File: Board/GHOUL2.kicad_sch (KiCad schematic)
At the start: 22 parts, among them U1 Teensy4.1, U2 DS18S20

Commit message: fixed more of JB's mistakes
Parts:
- R2: value 10K -> 15K
- R3: value 15K -> 10K
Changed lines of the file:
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@@
       (effects (font (size 1.27 1.27)) (justify left))
     )
-    (property "Value" "15K" (at 161.29 164.465 0)
+    (property "Value" "10K" (at 161.29 164.465 0)
       (effects (font (size 1.27 1.27)) (justify left))
     )
@@
       (effects (font (size 1.27 1.27)) (justify left))
     )
-    (property "Value" "10K" (at 161.29 154.305 0)
-      (effects (font (size 1.27 1.27)) (justify left))
-    )
+    (property "Value" "15K" (at 161.29 154.305 0)
+      (effects (font (size 1.27 1.27)) (justify left))
+    )

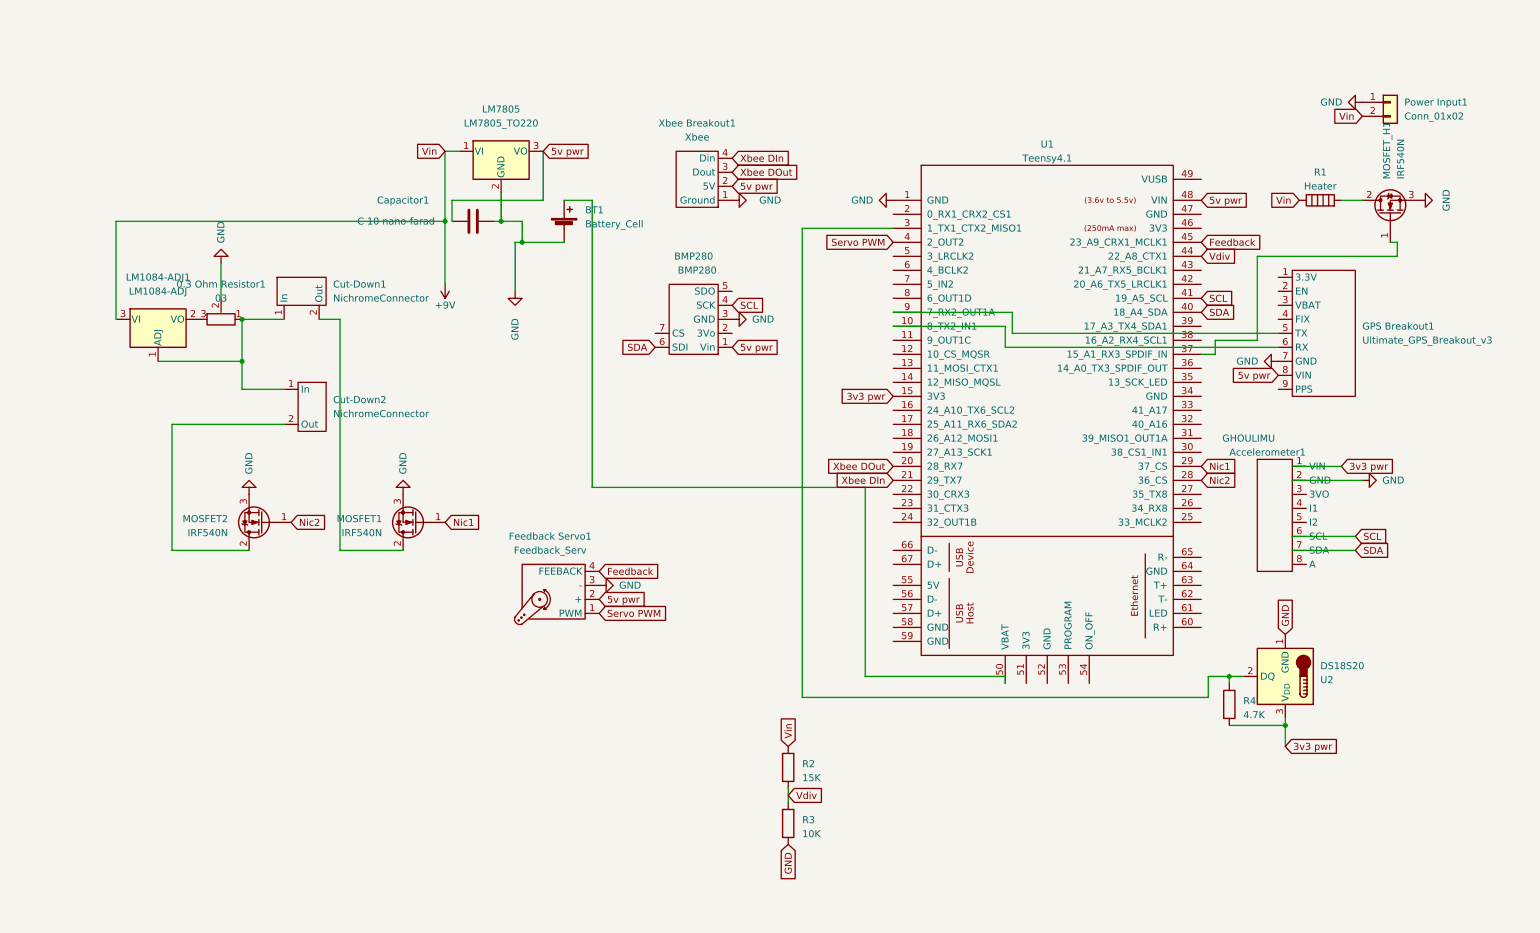
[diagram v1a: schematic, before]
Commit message: added gps, buck, pressure and clean up
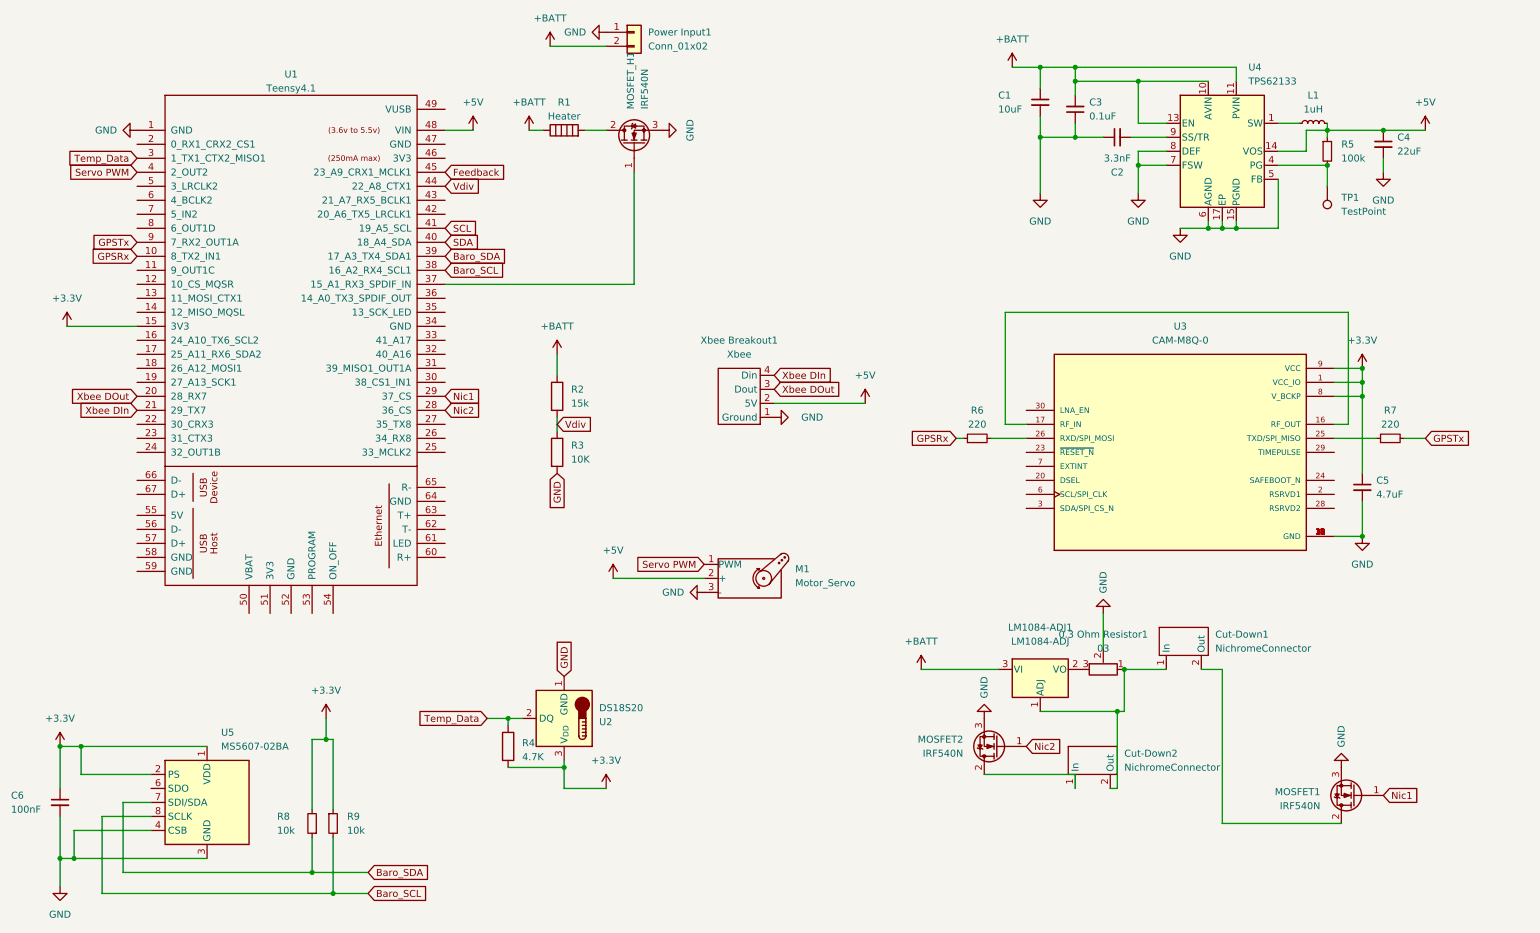
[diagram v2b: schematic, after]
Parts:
- removed Accelerometer1: GHOULIMU, GHOULFootPrints:GHOULIMU, symbol GHOUL:GHOULIMU
- removed BMP280: BMP280, GHOULFootPrints:BMP280, symbol GHOUL:BMP280
- removed BT1: Battery_Cell, Battery:BatteryHolder_Keystone_3000_1x12mm, symbol Device:Battery_Cell
- removed Capacitor1: C 10 nano-farad, GHOULFootPrints:GhoulResistor, symbol Device:C
- removed Feedback Servo1: Feedback_Serv, GHOULFootPrints:ServoPinout, symbol GHOUL:Feedback_Serv
- removed GPS Breakout1: Ultimate_GPS_Breakout_v3, GHOULFootPrints:Ultimate GPS Breakout v3, symbol GHOUL:Ultimate_GPS_Breakout_v3
- removed LM7805: LM7805_TO220, Package_TO_SOT_SMD:TO-263-3_TabPin2, symbol Regulator_Linear:LM7805_TO220
- added C1: 10uF, Capacitor_SMD:C_0603_1608Metric_Pad1.08x0.95mm_HandSolder, symbol Device:C_Small
- added C2: 3.3nF, Capacitor_SMD:C_0603_1608Metric_Pad1.08x0.95mm_HandSolder, symbol Device:C_Small
- added C3: 0.1uF, Capacitor_SMD:C_0603_1608Metric_Pad1.08x0.95mm_HandSolder, symbol Device:C_Small
- added C4: 22uF, Capacitor_SMD:C_0603_1608Metric_Pad1.08x0.95mm_HandSolder, symbol Device:C_Small
- added C5: 4.7uF, Capacitor_SMD:C_0603_1608Metric_Pad1.08x0.95mm_HandSolder, symbol Device:C_Small
- added C6: 100nF, Capacitor_SMD:C_0603_1608Metric_Pad1.08x0.95mm_HandSolder, symbol Device:C_Small
- added L1: 1uH, Inductor_SMD:L_Coilcraft_XxL4040, symbol Device:L_Small
- added M1: Motor_Servo, Connector_JST:JST_XH_B3B-XH-A_1x03_P2.50mm_Vertical, symbol Motor:Motor_Servo
- added R5: 100k, Resistor_SMD:R_0603_1608Metric_Pad0.98x0.95mm_HandSolder, symbol Device:R_Small
- added R6, R7: 220, Resistor_SMD:R_0603_1608Metric_Pad0.98x0.95mm_HandSolder, symbol Device:R_Small
- added R8, R9: 10k, Resistor_SMD:R_0603_1608Metric_Pad0.98x0.95mm_HandSolder, symbol Device:R_Small
- added TP1: TestPoint, TestPoint:TestPoint_Keystone_5000-5004_Miniature, symbol Connector:TestPoint
- added U3: CAM-M8Q-0, CAM-M8Q-0:LCC100P960X1400X210-31N, symbol CAM-M8Q-0:CAM-M8Q-0
- added U4: TPS62133, Package_DFN_QFN:VQFN-16-1EP_3x3mm_P0.5mm_EP1.68x1.68mm_ThermalVias, symbol Regulator_Switching:TPS62133
- added U5: MS5607-02BA, Package_LGA:LGA-8_3x5mm_P1.25mm, symbol Sensor_Pressure:MS5607-02BA
- R2: value 15K -> 15k
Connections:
- net GND: now also C1.2, C2.1, C3.1, C4.2, C5.2, C6.2, M1.3 (-), U3.10 (GND), U3.11 (GND), U3.12 (GND), U3.13 (GND), U3.14 (GND), U3.15 (GND), U3.18 (GND), U3.19 (GND), U3.21 (GND), U3.22 (GND), U3.27 (GND), U3.31 (GND), U3.4 (GND), U3.5 (GND), U4.15 (PGND), U4.16 (PGND), U4.17 (EP), U4.5 (FB), U4.6 (AGND), U4.7 (FSW), U4.8 (DEF), U5.3 (GND), U5.4 (CSB), U5.5 (CSB)
- net Servo PWM: now also M1.1 (PWM)
- net at 0.3 Ohm Resistor1.1, Cut-Down1.1 (In), LM1084-ADJ1.1 (ADJ): now also Cut-Down2.2 (Out); no longer Cut-Down2.1 (In)
- net at MOSFET2.2 (D): now also Cut-Down2.1 (In); no longer Cut-Down2.2 (Out)
- net Temp_Data: now reaches R4.1, U1.3 (1_TX1_CTX2_MISO1), U2.2 (DQ)
- net GPSTx: now reaches U1.9 (7_RX2_OUT1A)
- net GPSTx: now also R7.2
- net GPSRx: now reaches U1.10 (8_TX2_IN1)
- net GPSRx: now also R6.1
- net Baro_SCL: now reaches U1.38 (16_A2_RX4_SCL1)
- net Baro_SCL: now also R9.2, U5.8 (SCLK)
- net Baro_SDA: now reaches U1.39 (17_A3_TX4_SDA1)
- net Baro_SDA: now also R8.1, U5.7 (SDI/SDA)
- net +9V renamed +BATT
- net +BATT: now also C1.1, C3.2, U4.10 (AVIN), U4.11 (PVIN), U4.12 (PVIN), U4.13 (EN)
- net 3v3 pwr renamed +3.3V
- net +3.3V: now also C5.1, C6.1, R8.2, R9.1, U3.1 (VCC_IO), U3.8 (V_BCKP), U3.9 (VCC), U5.1 (VDD), U5.2 (PS)
- net 5v pwr renamed +5V
- net +5V: now also C4.1, L1.2, M1.2 (+), R5.1, U4.14 (VOS)
- new net: R5.2, TP1.1, U4.4 (PG)
- new net: L1.1, U4.1 (SW), U4.2 (SW), U4.3 (SW)
- new net: R6.2, U3.26 (RXD/SPI_MOSI)
- new net: U3.16 (RF_OUT), U3.17 (RF_IN)
- new net: R7.1, U3.25 (TXD/SPI_MISO)
- new net: C2.2, U4.9 (SS/TR)
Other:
- moved on the sheet: 0.3 Ohm Resistor1, Cut-Down1, Cut-Down2, LM1084-ADJ1, MOSFET1, MOSFET2, MOSFET_H1, Power Input1, R1, R2, R3, R4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
